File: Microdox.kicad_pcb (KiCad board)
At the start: 2 copper layers, 153.3 x 135.5 mm, 47 parts, among them P1 USB, P2 CONN_01X03, SW0:0 SWITCH_DIODE, SW0:1 SWITCH_DIODE, SW0:2 SWITCH_DIODE, SW0:3 SWITCH_DIODE, SW0:4 SWITCH_DIODE, SW0:5 SWITCH_DIODE, SW0:6 SWITCH_DIODE, SW1:0 SWITCH_DIODE, SW1:1 SWITCH_DIODE, SW1:2 SWITCH_DIODE, SW1:3 SWITCH_DIODE, SW1:4 SWITCH_DIODE, SW1:5 SWITCH_DIODE, SW2:0 SWITCH_DIODE, SW2:1 SWITCH_DIODE, SW2:2 SWITCH_DIODE, SW2:3 SWITCH_DIODE, SW2:4 SWITCH_DIODE, SW2:5 SWITCH_DIODE, SW2:6 SWITCH_DIODE, SW3:0 SWITCH_DIODE, SW3:1 SWITCH_DIODE, SW3:2 SWITCH_DIODE, SW3:3 SWITCH_DIODE, SW3:4 SWITCH_DIODE, SW3:5 SWITCH_DIODE, SW3:6 SWITCH_DIODE, SW4:5 SWITCH_DIODE, SW4:6 SWITCH_DIODE

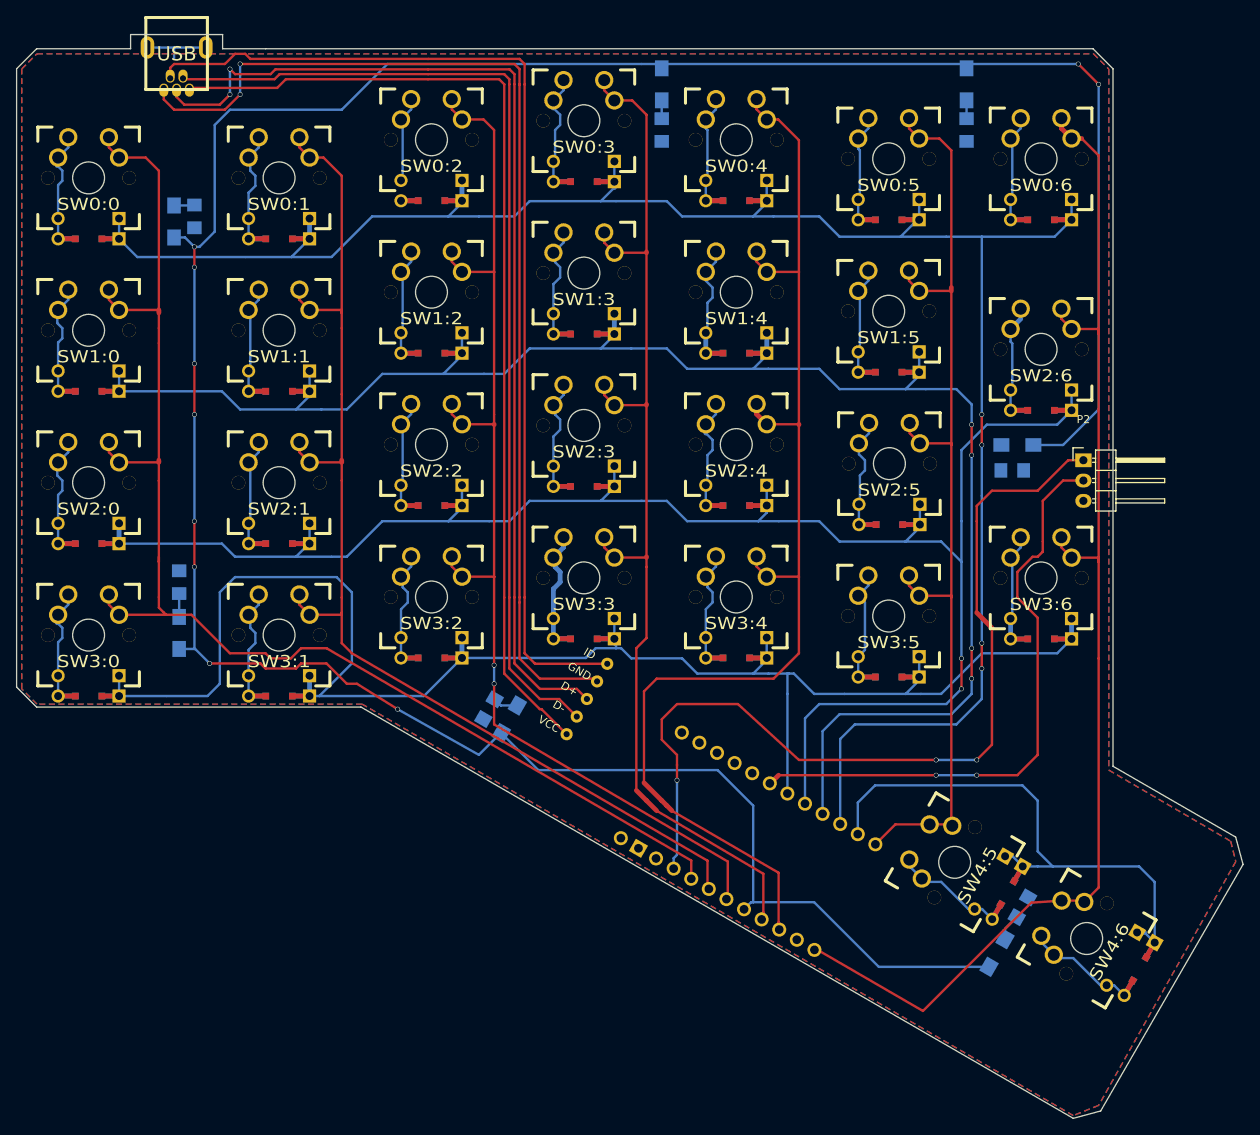
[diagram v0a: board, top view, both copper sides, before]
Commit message: Add version without backlighting
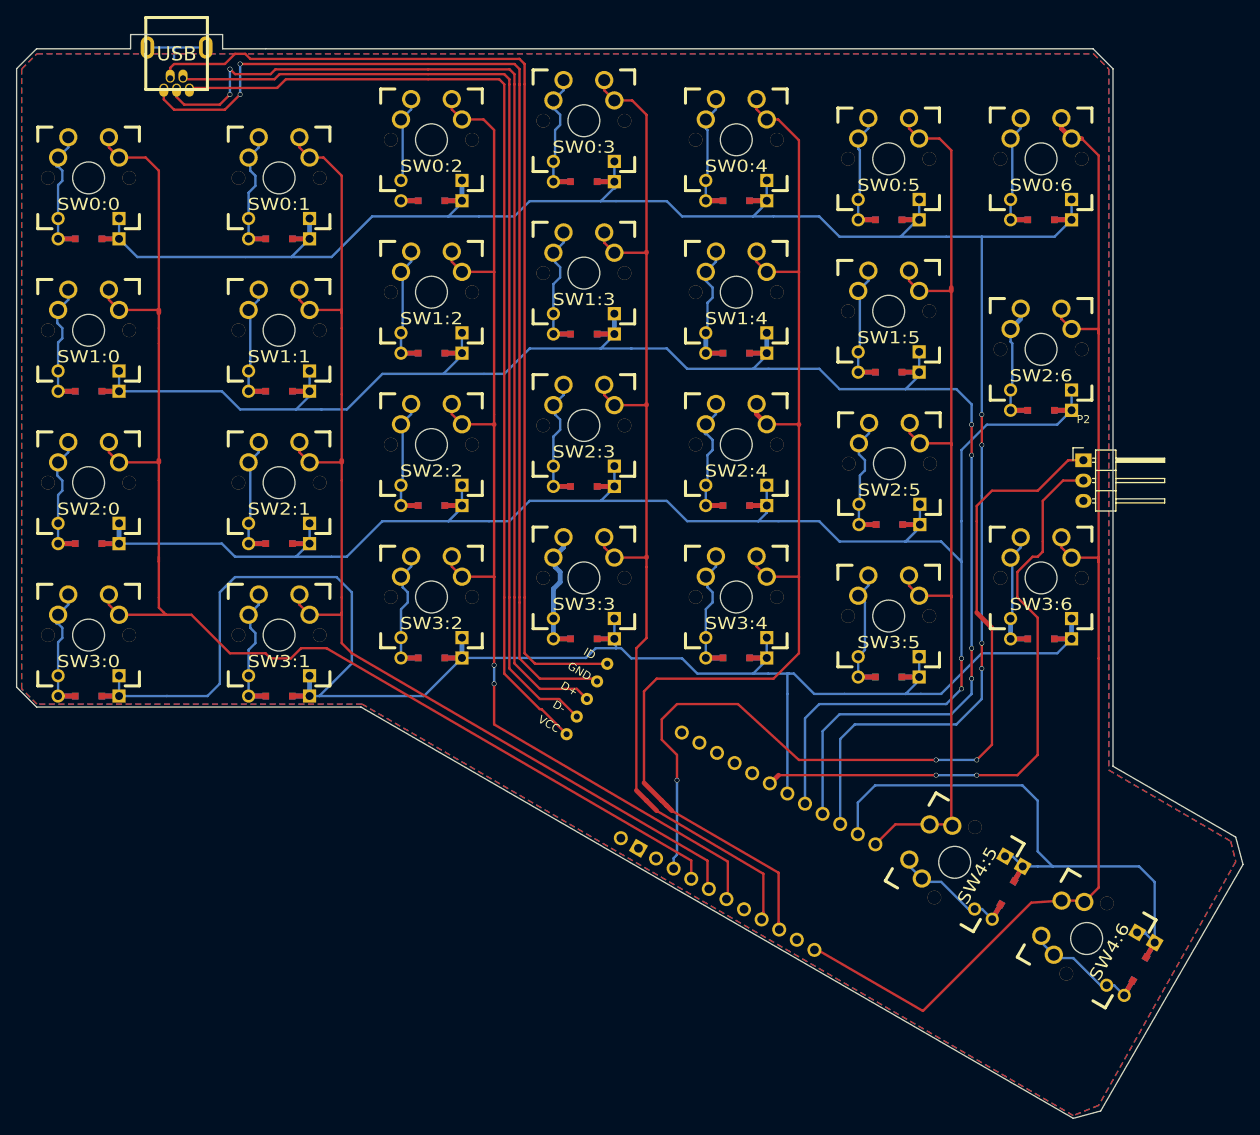
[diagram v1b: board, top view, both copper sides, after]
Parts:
- removed D30, D31, D32, D33, D34, D35, D36: LED, LEDs:LED_1206
- removed R1, R2, R3, R4, R5, R6, R7: 100R, Resistors_SMD:R_1206_HandSoldering
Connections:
- PM1 pad 19: /LED+ -> (no net)
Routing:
- net /LED+: track 364.0 -> 0.00 mm, vias 10 -> 0
- net Net-(D33-Pad2): track 3.36 -> 0.00 mm
- net Net-(D36-Pad2): track 3.15 -> 0.00 mm
- net Net-(D35-Pad2): track 2.93 -> 0.00 mm
- net Net-(D34-Pad2): track 2.56 -> 0.00 mm
- net Net-(D32-Pad2): track 2.30 -> 0.00 mm
- net Net-(D31-Pad2): track 2.30 -> 0.00 mm

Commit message: Add more vias
Fix non-connectivity island
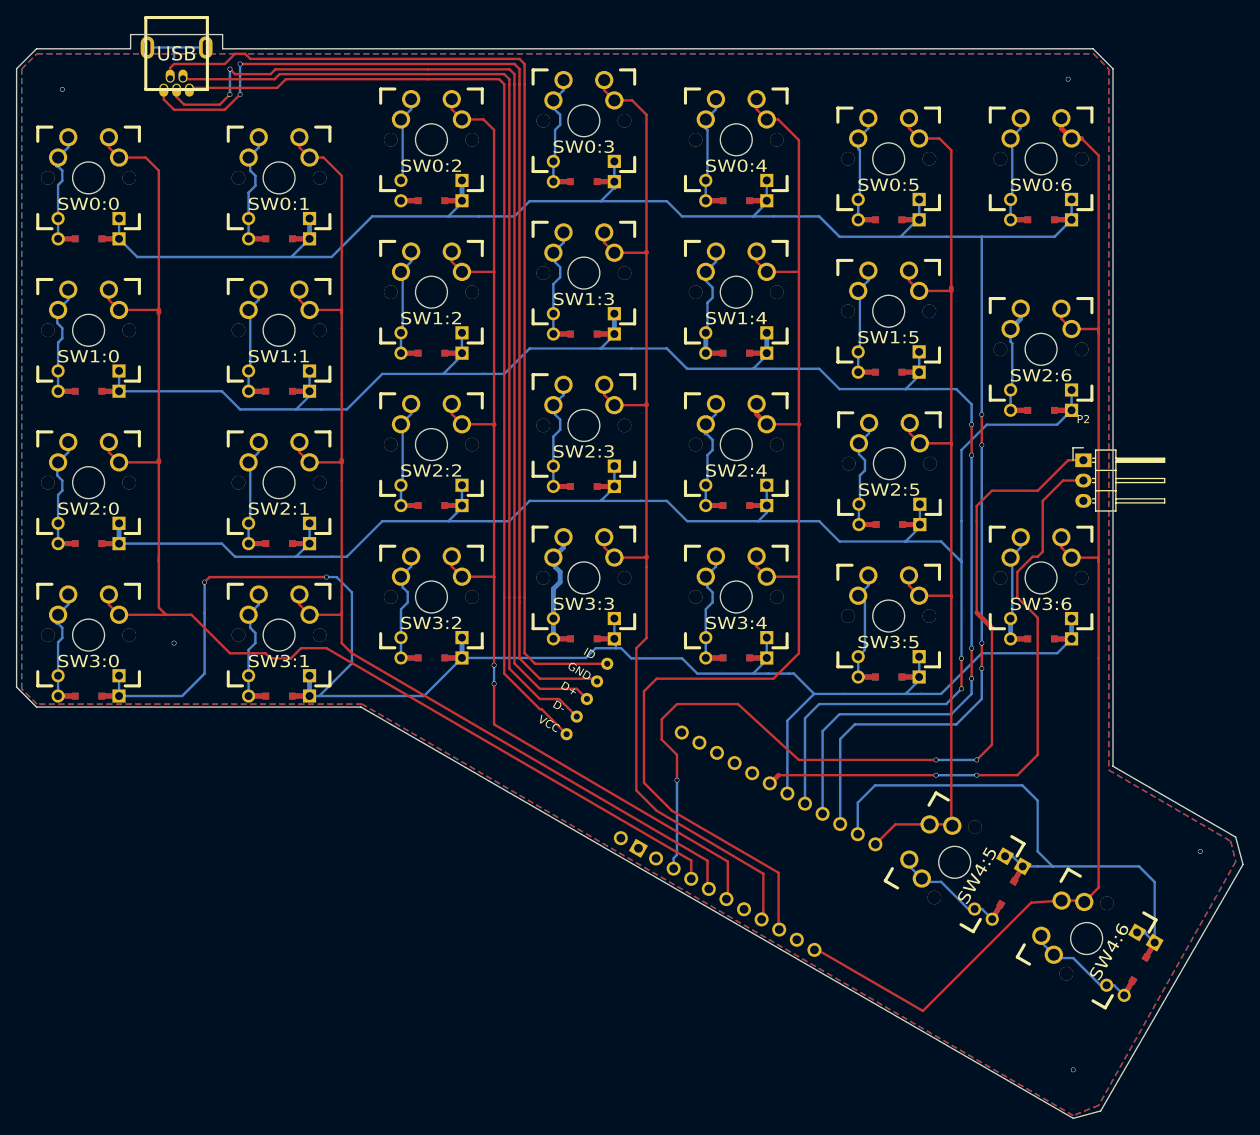
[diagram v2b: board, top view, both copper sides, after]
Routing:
- net /ROW3: track 200.8 -> 199.4 mm, vias 0 -> 2
- net (no net): vias 0 -> 5
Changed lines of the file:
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@@
     (links 215)
     (no_connects 11)
-    (area -0.075001 -1.853001 153.381001 133.773001)
+    (area -0.827001 -4.394481 153.381001 133.773001)
     (thickness 1.6)
     (drawings 17)
-    (tracks 739)
+    (tracks 747)
     (zones 0)
     (modules 33)
@@
     (visible_elements FFFFFFFF)
     (pcbplotparams
-      (layerselection 0x00030_80000001)
-      (usegerberextensions false)
+      (layerselection 0x01030_80000001)
+      (usegerberextensions true)
       (excludeedgelayer true)
       (linewidth 0.100000)
@@
       (outputformat 1)
       (mirror false)
-      (drillshape 1)
+      (drillshape 0)
       (scaleselection 1)
-      (outputdirectory ""))
+      (outputdirectory gerber/))
   )
   (net 0 "")
@@
   (gr_line (start 2.5 82.289) (end 43.051 82.289) (angle 90) (layer Edge.Cuts) (width 0.15))
   (gr_line (start 0 2.5) (end 0 79.789) (angle 90) (layer Edge.Cuts) (width 0.15))
+  (via (at 147.955 100.33) (size 0.6) (drill 0.5) (layers F.Cu B.Cu) (net 0))
+  (via (at 132.08 127.635) (size 0.6) (drill 0.5) (layers F.Cu B.Cu) (net 0))
+  (via (at 19.685 74.295) (size 0.6) (drill 0.5) (layers F.Cu B.Cu) (net 0))
+  (via (at 131.445 3.81) (size 0.6) (drill 0.5) (layers F.Cu B.Cu) (net 0))
+  (via (at 5.715 5.08) (size 0.6) (drill 0.5) (layers F.Cu B.Cu) (net 0))
   (segment (start 16.35256 -0.15494) (end 19.685 -0.15494) (width 0.3) (layer B.Cu) (net 1))
   (segment (start 19.685 -0.15494) (end 19.685 1.27) (width 0.3) (layer B.Cu) (net 1))
@@
   (segment (start 123.563409 100.935443) (end 124.493114 100.935443) (width 0.3) (layer B.Cu) (net 4))
   (segment (start 124.493114 100.935443) (end 125.763114 102.205443) (width 0.3) (layer B.Cu) (net 4))
-  (segment (start 18.784 80.911) (end 23.864 80.911) (width 0.3) (layer B.Cu) (net 5))
-  (segment (start 25.4 67.945) (end 27.305 66.04) (width 0.3) (layer B.Cu) (net 5))
-  (segment (start 25.4 79.375) (end 25.4 67.945) (width 0.3) (layer B.Cu) (net 5))
-  (segment (start 23.864 80.911) (end 25.4 79.375) (width 0.3) (layer B.Cu) (net 5))
-  (segment (start 37.834 80.911) (end 50.908 80.911) (width 0.3) (layer B.Cu) (net 5))
-  (segment (start 36.62 80.911) (end 37.834 80.911) (width 0.3) (layer B.Cu) (net 5))
-  (segment (start 27.305 66.04) (end 40.005 66.04) (width 0.3) (layer B.Cu) (net 5))
-  (segment (start 37.834 80.911) (end 41.91 76.835) (width 0.3) (layer B.Cu) (net 5))
+  (segment (start 96.349852 93.095886) (end 96.349852 83.990148) (width 0.3) (layer B.Cu) (net 5) (status 400000))
+  (segment (start 96.349852 83.990148) (end 99.695 80.645) (width 0.3) (layer B.Cu) (net 5))
+  (segment (start 23.495 70.485) (end 23.495 66.675) (width 0.3) (layer B.Cu) (net 5))
+  (segment (start 20.689 80.911) (end 23.495 78.105) (width 0.3) (layer B.Cu) (net 5))
+  (segment (start 23.495 78.105) (end 23.495 70.485) (width 0.3) (layer B.Cu) (net 5))
   (segment (start 41.91 67.945) (end 41.91 76.835) (width 0.3) (layer B.Cu) (net 5))
   (segment (start 40.005 66.04) (end 41.91 67.945) (width 0.3) (layer B.Cu) (net 5))
-  (segment (start 18.784 80.911) (end 12.808 80.911) (width 0.3) (layer B.Cu) (net 5))
+  (segment (start 38.735 66.04) (end 40.005 66.04) (width 0.3) (layer B.Cu) (net 5))
+  (via (at 38.735 66.04) (size 0.6) (drill 0.5) (layers F.Cu B.Cu) (net 5))
+  (segment (start 24.765 66.04) (end 38.735 66.04) (width 0.3) (layer F.Cu) (net 5))
+  (segment (start 37.834 80.911) (end 41.91 76.835) (width 0.3) (layer B.Cu) (net 5))
+  (segment (start 20.689 80.911) (end 12.808 80.911) (width 0.3) (layer B.Cu) (net 5))
+  (segment (start 24.13 66.04) (end 24.765 66.04) (width 0.3) (layer F.Cu) (net 5))
+  (segment (start 23.495 66.675) (end 24.13 66.04) (width 0.3) (layer F.Cu) (net 5))
+  (via (at 23.495 66.675) (size 0.6) (drill 0.5) (layers F.Cu B.Cu) (net 5))
+  (segment (start 37.834 80.911) (end 50.908 80.911) (width 0.3) (layer B.Cu) (net 5))
+  (segment (start 50.908 80.911) (end 55.67 76.149) (width 0.3) (layer B.Cu) (net 5))
+  (segment (start 36.62 80.911) (end 37.834 80.911) (width 0.3) (layer B.Cu) (net 5))
   (segment (start 12.808 78.371) (end 12.808 80.911) (width 0.3) (layer B.Cu) (net 5))
   (segment (start 36.62 80.911) (end 36.62 78.371) (width 0.6) (layer B.Cu) (net 5))
   (segment (start 55.67 76.149) (end 71.12 76.149) (width 0.3) (layer B.Cu) (net 5))
-  (segment (start 50.908 80.911) (end 55.67 76.149) (width 0.3) (layer B.Cu) (net 5))
   (segment (start 55.67 73.609) (end 55.67 76.149) (width 0.6) (layer B.Cu) (net 5))
   (segment (start 74.93 74.93) (end 74.93 73.968) (width 0.3) (layer B.Cu) (net 5))
@@
   (segment (start 103.505 80.645) (end 99.695 80.645) (width 0.3) (layer B.Cu) (net 5))
   (segment (start 103.505 80.645) (end 111.125 80.645) (width 0.3) (layer B.Cu) (net 5))
-  (segment (start 96.349852 78.105) (end 96.52 78.105) (width 0.3) (layer B.Cu) (net 5))
-  (segment (start 96.349852 80.645) (end 96.349852 78.105) (width 0.3) (layer B.Cu) (net 5))
   (segment (start 92.075 78.105) (end 93.98 78.105) (width 0.3) (layer B.Cu) (net 5))
   (segment (start 93.98 78.105) (end 96.52 78.105) (width 0.3) (layer B.Cu) (net 5))
-  (segment (start 96.349852 93.095886) (end 96.349852 80.645) (width 0.3) (layer B.Cu) (net 5) (status 10))
   (segment (start 113.03 80.645) (end 115.57 80.645) (width 0.3) (layer B.Cu) (net 5))
   (segment (start 111.125 80.645) (end 113.03 80.645) (width 0.3) (layer B.Cu) (net 5))
@@
   (segment (start 78.4225 91.7575) (end 78.4225 80.3275) (width 0.3) (layer F.Cu) (net 10))
   (segment (start 78.4225 80.3275) (end 80.01 78.74) (width 0.3) (layer F.Cu) (net 10))
-  (segment (start 78.4225 91.7575) (end 80.645 93.98) (width 0.6) (layer F.Cu) (net 10))
+  (segment (start 78.4225 91.7575) (end 80.645 93.98) (width 0.3) (layer F.Cu) (net 10))
   (segment (start 95.328966 109.298966) (end 95.25 109.22) (width 0.3) (layer F.Cu) (net 10) (status 10))
   (segment (start 95.25 109.22) (end 95.25 103.002907) (width 0.3) (layer F.Cu) (net 10))
-  (segment (start 81.915 95.25) (end 81.28 94.615) (width 0.6) (layer F.Cu) (net 10))
+  (segment (start 81.915 95.25) (end 81.28 94.615) (width 0.3) (layer F.Cu) (net 10))
   (segment (start 94.615 78.74) (end 97.79 75.565) (width 0.3) (layer F.Cu) (net 10))
   (segment (start 94.615 78.74) (end 80.01 78.74) (width 0.3) (layer F.Cu) (net 10))
   (segment (start 97.79 66.04) (end 97.79 75.565) (width 0.3) (layer F.Cu) (net 10))
-  (segment (start 81.28 94.615) (end 80.645 93.98) (width 0.6) (layer F.Cu) (net 10))
+  (segment (start 81.28 94.615) (end 80.645 93.98) (width 0.3) (layer F.Cu) (net 10))
   (segment (start 95.25 103.002907) (end 81.915 95.25) (width 0.3) (layer F.Cu) (net 10))
   (segment (start 95.328966 110.104114) (end 95.328966 109.298966) (width 0.3) (layer F.Cu) (net 10) (status 30))
@@
   (segment (start 78.74 64.77) (end 78.74 63.5) (width 0.3) (layer F.Cu) (net 12))
   (segment (start 78.74 64.77) (end 78.74 73.66) (width 0.3) (layer F.Cu) (net 12))
-  (segment (start 77.47 92.71) (end 78.74 93.98) (width 0.6) (layer F.Cu) (net 12))
-  (segment (start 78.74 93.98) (end 80.01 95.25) (width 0.6) (layer F.Cu) (net 12))
+  (segment (start 77.47 92.71) (end 78.74 93.98) (width 0.3) (layer F.Cu) (net 12))
+  (segment (start 78.74 93.98) (end 80.01 95.25) (width 0.3) (layer F.Cu) (net 12))
   (segment (start 78.74 63.598) (end 78.74 63.5) (width 0.6) (layer F.Cu) (net 12))
   (segment (start 78.74 44.45) (end 78.74 63.5) (width 0.3) (layer F.Cu) (net 12))
